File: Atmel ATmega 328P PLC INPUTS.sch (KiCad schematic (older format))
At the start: 46 parts

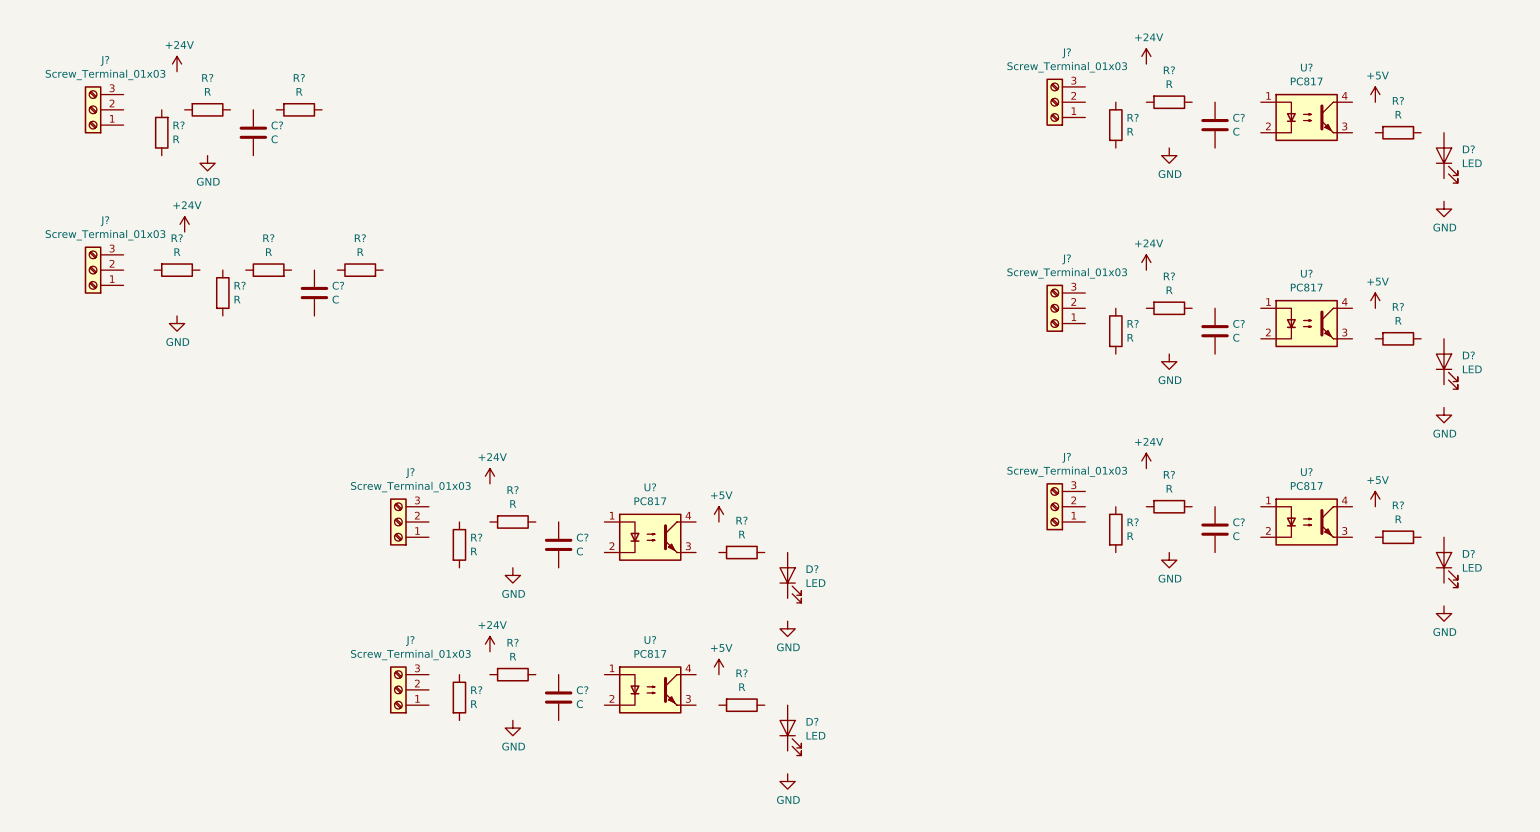
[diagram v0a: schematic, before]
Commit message: Added all schematic components, annotated and asigned!
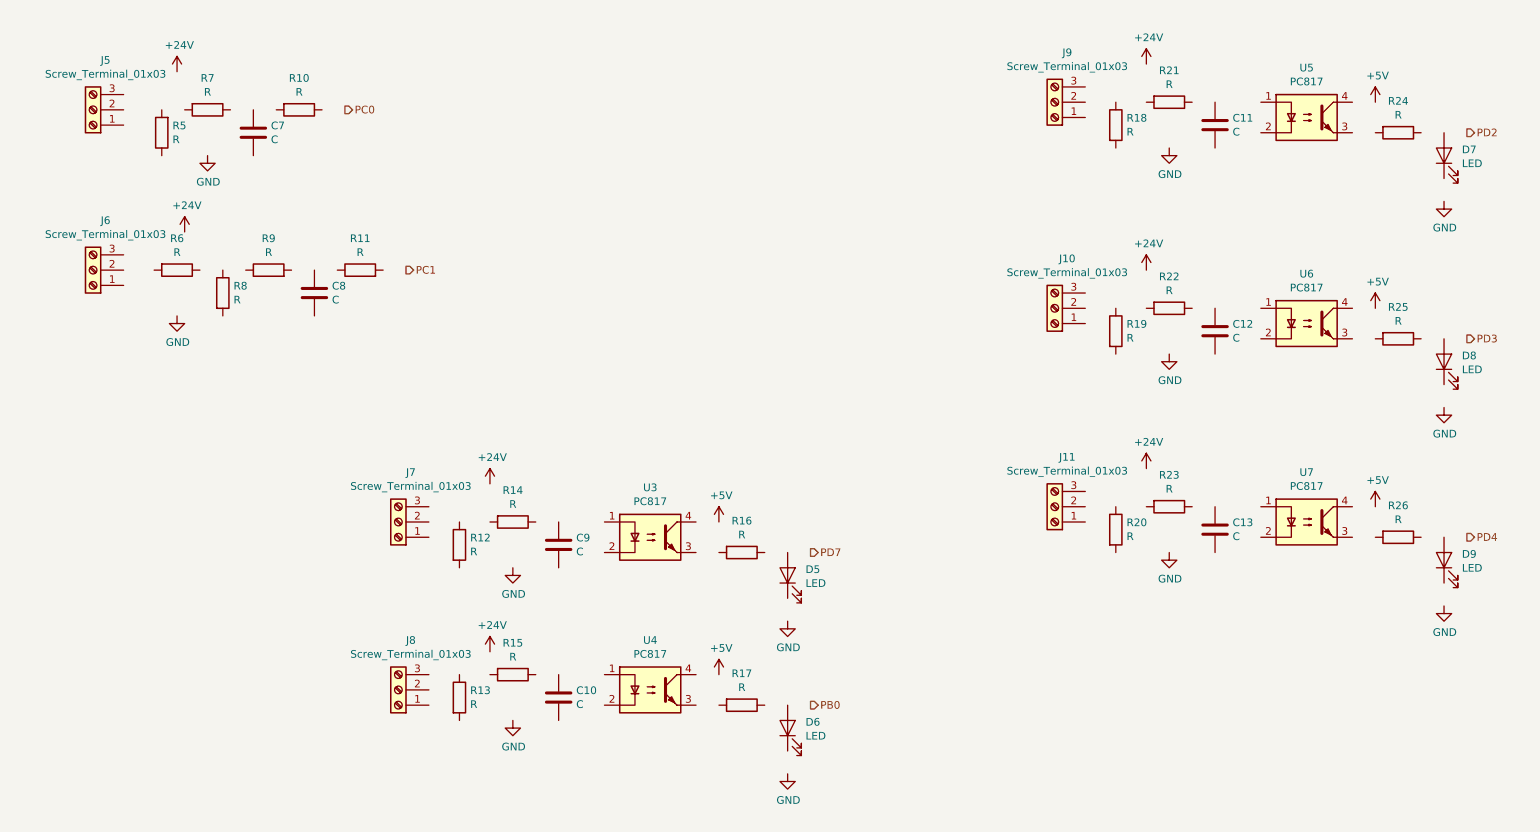
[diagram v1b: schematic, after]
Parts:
- C10, C11, C12, C13, C7, C8, C9: renamed from C?; footprint (none) -> Capacitor_SMD:C_0603_1608Metric_Pad1.05x0.95mm_HandSolder
- D5, D6, D7, D8, D9: renamed from D?; footprint (none) -> LED_SMD:LED_0603_1608Metric_Pad1.05x0.95mm_HandSolder
- J10, J11, J5, J6, J7, J8, J9: renamed from J?; footprint (none) -> TerminalBlock_Phoenix:TerminalBlock_Phoenix_PT-1,5-3-5.0-H_1x03_P5.00mm_Horizontal
- R10, R11, R12, R13, R14, R15, R16, R17, R18, R19, R20, R21, R22, R23, R24, R25, R26, R5, R6, R7, R8, R9: renamed from R?; footprint (none) -> Resistor_SMD:R_0603_1608Metric_Pad1.05x0.95mm_HandSolder
- U3, U4, U5, U6, U7: renamed from U?; footprint Package_DIP:DIP-4_W7.62mm -> kicad-open-modules-master:HCPL-817-300E

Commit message: Finished schematic with all elements.
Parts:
- C10, C11, C12, C13, C7, C8, C9: value C -> 1uF 35V
- D5, D6, D7, D8, D9: value LED -> GREEN
- R10, R14, R15, R21, R22, R23: value R -> 2k2
- R12, R13, R18, R19, R20, R6, R8: value R -> 4k7
- R16, R17, R24, R25, R26: value R -> 220R
- R5: value R -> 250R
- R7: value R -> 10K
- R9: value R -> 10k
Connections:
- net +24V: now also J10.3 (Pin_3), J11.3 (Pin_3), J5.3 (Pin_3), J6.3 (Pin_3), J7.3 (Pin_3), J8.3 (Pin_3), J9.3 (Pin_3), R13.1, R15.2
- net +5V: now also U3.4, U4.4, U5.4, U6.4, U7.4
- net GND: now also C11.2, C12.2, C13.2, C7.2, C8.2, C9.2, D5.1 (K), D6.1 (K), D7.1 (K), D8.1 (K), D9.1 (K), J10.1 (Pin_1), J11.1 (Pin_1), J5.1 (Pin_1), J6.1 (Pin_1), J7.1 (Pin_1), J8.1 (Pin_1), J9.1 (Pin_1), R12.2, R18.2, R19.2, R20.2, R5.2, R8.2, U3.2, U5.2, U6.2, U7.2
- net PB0: now also D6.2 (A), R17.1
- net PC0: now also R10.1
- net PC1: now also R11.2
- net PD2: now also D7.2 (A), R24.1
- net PD3: now also D8.2 (A), R25.1
- net PD4: now also D9.2 (A), R26.1
- net PD7: now also D5.2 (A), R16.1
- net at R8.1: now also R6.1, R9.1
- net at R9.2: now also C8.1, R11.1
- net at R10.2: now also C7.1, R7.1
- net at C10.1: now also R15.1, U4.1
- net at C10.2: now also J8.2 (Pin_2), R13.2, U4.2
- net at U4.3: now also R17.2
- net at R16.2: now also U3.3
- net at U3.1: now also C9.1, R14.1
- net at R24.2: now also U5.3
- net at U5.1: now also C11.1, R21.1
- net at J9.2 (Pin_2): now also R18.1, R21.2
- net at J7.2 (Pin_2): now also R12.1, R14.2
- net at R7.2: now also J5.2 (Pin_2), R5.1
- net at R6.2: now also J6.2 (Pin_2)
- net at R25.2: now also U6.3
- net at U6.1: now also C12.1, R22.1
- net at J10.2 (Pin_2): now also R19.1, R22.2
- net at R26.2: now also U7.3
- net at U7.1: now also C13.1, R23.1
- net at J11.2 (Pin_2): now also R20.1, R23.2
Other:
- note added: "0 - 10 V input"
- note added: "24V pushbutton inputs"
- note added: "4 - 20 mA (0 - 20 mA) input\n"
- note added: "Analog inputs"
- note added: "NPN\n"
- note added: "PNP"
- note added: "PNP and NPN inputs"
